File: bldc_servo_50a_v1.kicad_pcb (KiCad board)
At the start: 2 copper layers, 50 parts, among them J1 CAN_JST-1, J2 CAN_JST-2, J3 Encoder_JST_1, J4 Encoder_JST_2, J5 Fan_JST, Q1 BSC010N04LS, Q2 BSC010N04LS, Q3 BSC010N04LS, Q4 BSC010N04LS, Q5 BSC010N04LS, Q6 BSC010N04LS, U1 LM3480-3.3_Yet to decide, U2 SN65HVD230, U3 STM32G431CBT6

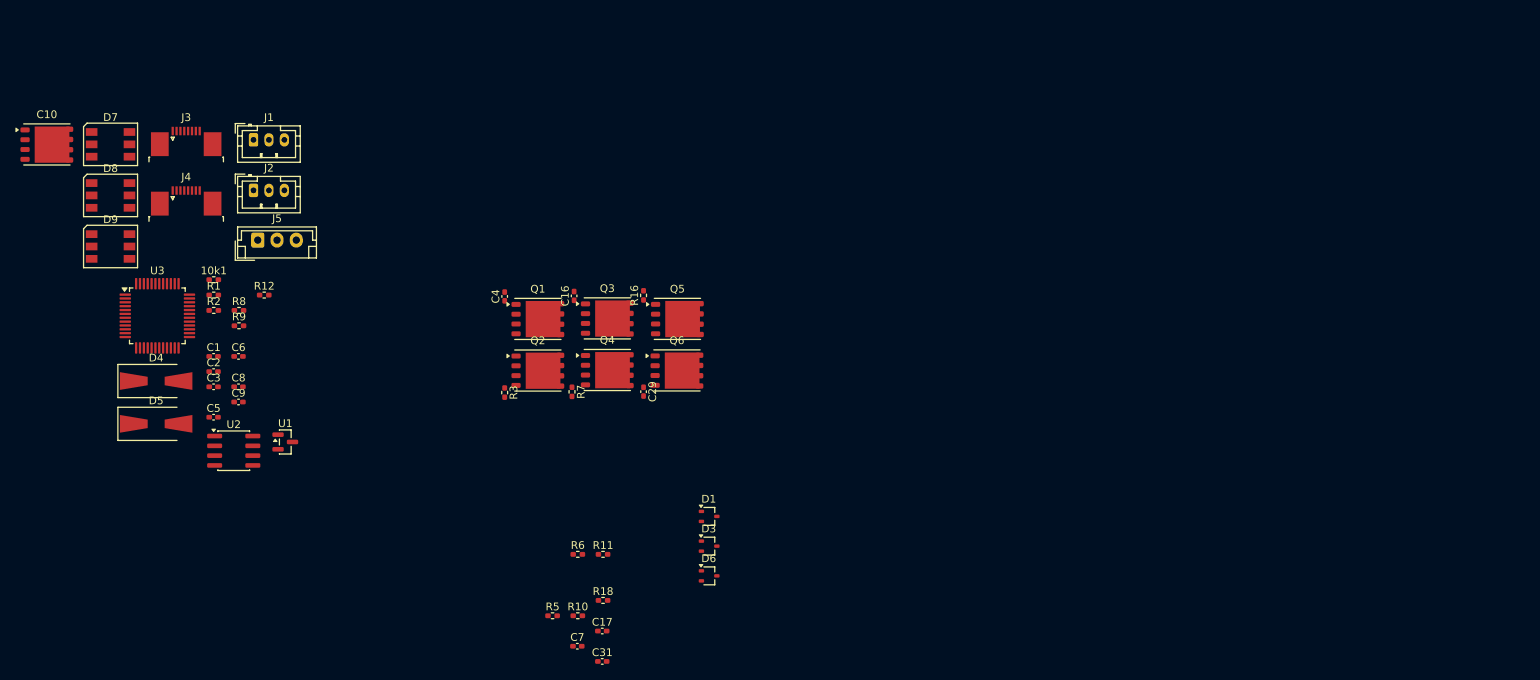
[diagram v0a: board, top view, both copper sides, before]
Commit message: FETs placed
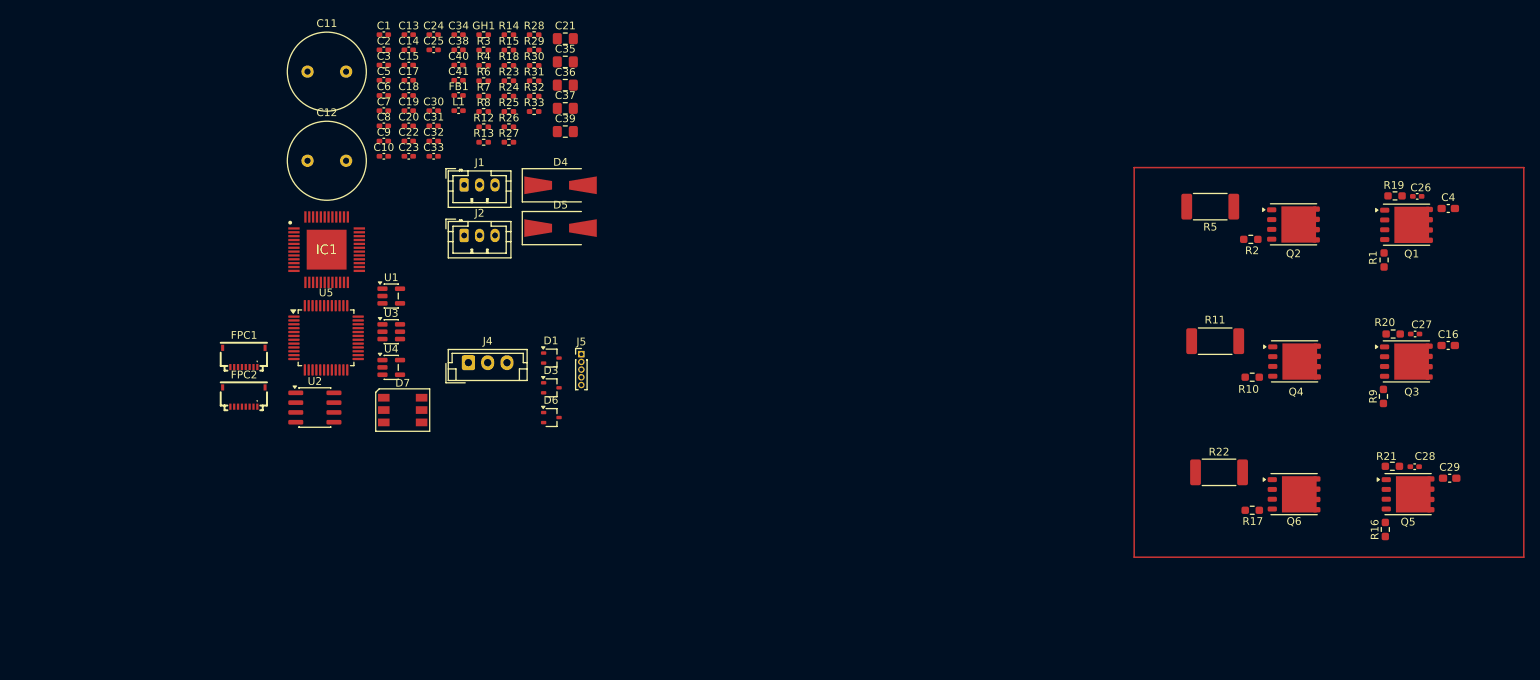
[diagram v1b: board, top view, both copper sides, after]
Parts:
- removed 10k1: R_Small, Resistor_SMD:R_0402_1005Metric_Pad0.72x0.64mm_HandSolder
- removed D8, D9: WS2812, LED_SMD:LED_WS2812_PLCC6_5.0x5.0mm_P1.6mm
- removed J3: Encoder_JST_1, Connector_FFC-FPC:TE_0-1734839-8_1x08-1MP_P0.5mm_Horizontal
- added C11: 470u, Capacitor_THT:C_Radial_D10.0mm_H16.0mm_P5.00mm, F.Cu at (74.4, 25.0)
- added C12: 470u, Capacitor_THT:C_Radial_D10.0mm_H16.0mm_P5.00mm, F.Cu at (74.4, 36.5)
- added C13: 1u, Capacitor_SMD:C_0402_1005Metric_Pad0.74x0.62mm_HandSolder, F.Cu at (87.6, 20.2)
- added C14: 0.1u, Capacitor_SMD:C_0402_1005Metric_Pad0.74x0.62mm_HandSolder, F.Cu at (87.6, 22.2)
- added C15: 0.01u, Capacitor_SMD:C_0402_1005Metric_Pad0.74x0.62mm_HandSolder, F.Cu at (87.6, 24.1)
- added C18: 1u, Capacitor_SMD:C_0402_1005Metric_Pad0.74x0.62mm_HandSolder, F.Cu at (87.6, 28.1)
- added C19: 1u, Capacitor_SMD:C_0402_1005Metric_Pad0.74x0.62mm_HandSolder, F.Cu at (87.6, 30.1)
- added C20: 100n, Capacitor_SMD:C_0402_1005Metric_Pad0.74x0.62mm_HandSolder, F.Cu at (87.6, 32.0)
- added C21: 10u, Capacitor_SMD:C_0805_2012Metric_Pad1.18x1.45mm_HandSolder, F.Cu at (107.9, 20.7)
- added C22: 100n, Capacitor_SMD:C_0402_1005Metric_Pad0.74x0.62mm_HandSolder, F.Cu at (87.6, 34.0)
- added C23: 100n, Capacitor_SMD:C_0402_1005Metric_Pad0.74x0.62mm_HandSolder, F.Cu at (87.6, 36.0)
- added C24: 100n, Capacitor_SMD:C_0402_1005Metric_Pad0.74x0.62mm_HandSolder, F.Cu at (90.8, 20.2)
- added C25: 100n, Capacitor_SMD:C_0402_1005Metric_Pad0.74x0.62mm_HandSolder, F.Cu at (90.8, 22.2)
- added C26: 22n, Capacitor_SMD:C_0402_1005Metric_Pad0.74x0.62mm_HandSolder, F.Cu at (218.3, 41.2)
- added C27: 22n, Capacitor_SMD:C_0402_1005Metric_Pad0.74x0.62mm_HandSolder, F.Cu at (218.0, 59.0)
- added C28: 22n, Capacitor_SMD:C_0402_1005Metric_Pad0.74x0.62mm_HandSolder, F.Cu at (217.9, 76.2)
- added C30: 10n, Capacitor_SMD:C_0402_1005Metric_Pad0.74x0.62mm_HandSolder, F.Cu at (90.8, 30.1)
- added C32: 1u, Capacitor_SMD:C_0402_1005Metric_Pad0.74x0.62mm_HandSolder, F.Cu at (90.8, 34.0)
- added C33: 100n, Capacitor_SMD:C_0402_1005Metric_Pad0.74x0.62mm_HandSolder, F.Cu at (90.8, 36.0)
- added C34: 100n, Capacitor_SMD:C_0402_1005Metric_Pad0.74x0.62mm_HandSolder, F.Cu at (94.0, 20.2)
- added C35: 10u, Capacitor_SMD:C_0805_2012Metric_Pad1.18x1.45mm_HandSolder, F.Cu at (107.9, 23.7)
- added C36: 10u, Capacitor_SMD:C_0805_2012Metric_Pad1.18x1.45mm_HandSolder, F.Cu at (107.9, 26.8)
- added C37: 10u, Capacitor_SMD:C_0805_2012Metric_Pad1.18x1.45mm_HandSolder, F.Cu at (107.9, 29.8)
- added C38: 100n, Capacitor_SMD:C_0402_1005Metric_Pad0.74x0.62mm_HandSolder, F.Cu at (94.0, 22.2)
- added C39: 10u, Capacitor_SMD:C_0805_2012Metric_Pad1.18x1.45mm_HandSolder, F.Cu at (107.9, 32.8)
- added C40: 100n, Capacitor_SMD:C_0402_1005Metric_Pad0.74x0.62mm_HandSolder, F.Cu at (94.0, 24.1)
- added C41: 100n, Capacitor_SMD:C_0402_1005Metric_Pad0.74x0.62mm_HandSolder, F.Cu at (94.0, 26.1)
- added FB1: FB, Capacitor_SMD:C_0402_1005Metric_Pad0.74x0.62mm_HandSolder, F.Cu at (94.0, 28.1)
- added FPC1: External sensor, HCTL HC-FPC-05-09-8RLTAG_8pin connector:FPC-SMD_8P-P0.50_HC-FPC-05-09-8RLTAG, F.Cu at (66.2, 62.0)
- added FPC2: External sensor, HCTL HC-FPC-05-09-8RLTAG_8pin connector:FPC-SMD_8P-P0.50_HC-FPC-05-09-8RLTAG, F.Cu at (66.2, 67.2)
- added GH1: 10k, Resistor_SMD:R_0402_1005Metric_Pad0.72x0.64mm_HandSolder, F.Cu at (97.3, 20.2)
- added IC1: DRV8305NQPHPRQ1, DRV8305NQPHPRQ1:QFP50P900X900X120-49N, F.Cu at (76.9, 48.1)
- added L1: 3.3uH, Capacitor_SMD:C_0402_1005Metric_Pad0.74x0.62mm_HandSolder, F.Cu at (94.0, 30.1)
- added R13: 5k, Resistor_SMD:R_0402_1005Metric_Pad0.72x0.64mm_HandSolder, F.Cu at (97.3, 34.1)
- added R14: 34.8k, Resistor_SMD:R_0402_1005Metric_Pad0.72x0.64mm_HandSolder, F.Cu at (100.5, 20.2)
- added R15: 5k, Resistor_SMD:R_0402_1005Metric_Pad0.72x0.64mm_HandSolder, F.Cu at (100.5, 22.2)
- added R17: 10, Resistor_SMD:R_0603_1608Metric_Pad0.98x0.95mm_HandSolder, F.Cu at (196.9, 81.9)
- added R19: 10, Resistor_SMD:R_0603_1608Metric_Pad0.98x0.95mm_HandSolder, F.Cu at (215.4, 41.1)
- added R20: 10, Resistor_SMD:R_0603_1608Metric_Pad0.98x0.95mm_HandSolder, F.Cu at (215.2, 59.0)
- added R21: 10, Resistor_SMD:R_0603_1608Metric_Pad0.98x0.95mm_HandSolder, F.Cu at (215.1, 76.2)
- added R22: 1m, Resistor_SMD:R_2512_6332Metric_Pad1.40x3.35mm_HandSolder, F.Cu at (192.6, 76.9)
- added R23: 100k, Resistor_SMD:R_0402_1005Metric_Pad0.72x0.64mm_HandSolder, F.Cu at (100.5, 26.2)
- added R24: 13.7k, Resistor_SMD:R_0402_1005Metric_Pad0.72x0.64mm_HandSolder, F.Cu at (100.5, 28.2)
- added R25: 34.8k, Resistor_SMD:R_0402_1005Metric_Pad0.72x0.64mm_HandSolder, F.Cu at (100.5, 30.2)
- added R26: 5k, Resistor_SMD:R_0402_1005Metric_Pad0.72x0.64mm_HandSolder, F.Cu at (100.5, 32.2)
- added R27: 34.8k, Resistor_SMD:R_0402_1005Metric_Pad0.72x0.64mm_HandSolder, F.Cu at (100.5, 34.1)
- added R28: 5k, Resistor_SMD:R_0402_1005Metric_Pad0.72x0.64mm_HandSolder, F.Cu at (103.8, 20.2)
- added R29: 10k1, Resistor_SMD:R_0402_1005Metric_Pad0.72x0.64mm_HandSolder, F.Cu at (103.8, 22.2)
- added R30: 34.8k, Resistor_SMD:R_0402_1005Metric_Pad0.72x0.64mm_HandSolder, F.Cu at (103.8, 24.2)
- added R31: 5k, Resistor_SMD:R_0402_1005Metric_Pad0.72x0.64mm_HandSolder, F.Cu at (103.8, 26.2)
- added R32: 34.8k, Resistor_SMD:R_0402_1005Metric_Pad0.72x0.64mm_HandSolder, F.Cu at (103.8, 28.2)
- added R33: 5k, Resistor_SMD:R_0402_1005Metric_Pad0.72x0.64mm_HandSolder, F.Cu at (103.8, 30.2)
- added R4: 10k, Resistor_SMD:R_0402_1005Metric_Pad0.72x0.64mm_HandSolder, F.Cu at (97.3, 24.2)
- added U4: TPS2051BDBV, Package_TO_SOT_SMD:SOT-23-5, F.Cu at (85.3, 63.3)
- added U5: STM32G431CBT6, Package_QFP:LQFP-48_7x7mm_P0.5mm, F.Cu at (76.8, 59.5)
- C10: footprint Package_SON:Infineon_PG-TDSON-8_6.15x5.15mm -> Capacitor_SMD:C_0402_1005Metric_Pad0.74x0.62mm_HandSolder
- C16, C29, C4: footprint Capacitor_SMD:C_0402_1005Metric_Pad0.74x0.62mm_HandSolder -> Capacitor_SMD:C_0603_1608Metric_Pad1.08x0.95mm_HandSolder
- J4: value Encoder_JST_2 -> Fan_JST; footprint Connector_FFC-FPC:TE_0-1734839-8_1x08-1MP_P0.5mm_Horizontal -> Connector_JST:JST_EH_B3B-EH-A_1x03_P2.50mm_Vertical
- J5: value Fan_JST -> SWD; footprint Connector_JST:JST_EH_B3B-EH-A_1x03_P2.50mm_Vertical -> Connector_PinHeader_1.00mm:PinHeader_1x05_P1.00mm_Vertical
- R1, R2: value 10k -> 10; footprint Resistor_SMD:R_0402_1005Metric_Pad0.72x0.64mm_HandSolder -> Resistor_SMD:R_0603_1608Metric_Pad0.98x0.95mm_HandSolder
- R10: value 34.8k -> 10; footprint Resistor_SMD:R_0402_1005Metric_Pad0.72x0.64mm_HandSolder -> Resistor_SMD:R_0603_1608Metric_Pad0.98x0.95mm_HandSolder
- R11: value 5k -> 1m; footprint Resistor_SMD:R_0402_1005Metric_Pad0.72x0.64mm_HandSolder -> Resistor_SMD:R_2512_6332Metric_Pad1.40x3.35mm_HandSolder
- R12: value 120 -> 34.8k
- R16: value 1m -> 10; footprint Resistor_SMD:R_0402_1005Metric_Pad0.72x0.64mm_HandSolder -> Resistor_SMD:R_0603_1608Metric_Pad0.98x0.95mm_HandSolder
- R18: value 5k -> 120
- R3: value 1m -> 10k
- R5: value 34.8k -> 1m; footprint Resistor_SMD:R_0402_1005Metric_Pad0.72x0.64mm_HandSolder -> Resistor_SMD:R_2512_6332Metric_Pad1.40x3.35mm_HandSolder
- R6: value 5k -> 100
- R7: value 1m -> 34.8k
- R8: value 34.8k -> 5k
- R9: value 5k -> 10; footprint Resistor_SMD:R_0402_1005Metric_Pad0.72x0.64mm_HandSolder -> Resistor_SMD:R_0603_1608Metric_Pad0.98x0.95mm_HandSolder
- U1: value LM3480-3.3_Yet to decide -> TLV75533PDBV; footprint Package_TO_SOT_SMD:SOT-23 -> Package_TO_SOT_SMD:SOT-23-5
- U3: value STM32G431CBT6 -> LMR51430; footprint Package_QFP:LQFP-48_7x7mm_P0.5mm -> Package_TO_SOT_SMD:SOT-23-6
- moved R1 151.8 mm to (214.0, 49.4), turned to 90 degrees
- moved R9 148.6 mm to (213.9, 67.1), turned to 90 degrees
- moved R2 134.7 mm to (196.7, 46.7)
- moved C4 122.8 mm to (222.3, 42.7), turned to 0 degrees
- moved C16 113.5 mm to (222.3, 60.5), turned to 0 degrees
- moved Q1 113.2 mm to (216.9, 44.9)
- moved C29 105.1 mm to (222.5, 77.7), turned to 0 degrees
- moved Q3 103.7 mm to (216.9, 62.6)
- moved R16 100.8 mm to (214.1, 84.3)
- moved R5 100.4 mm to (191.4, 42.5), turned to 180 degrees
- moved Q2 99.8 mm to (202.2, 44.8)
- moved Q5 97.4 mm to (217.1, 79.8)
- moved R10 92.7 mm to (196.9, 64.6)
- moved Q4 89.1 mm to (202.4, 62.6)
- moved R11 84.0 mm to (192.1, 59.9), turned to 180 degrees
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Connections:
- C17 pad 1: /BSENSE -> +3.3V
- C17 pad 2: GND -> Net-(U1-GND)
- D7 pad 1: Net-(D7-DOUT) -> unconnected-(D7-DOUT-Pad1)
- J4 pad 1: +5V -> /FAN
- J4 pad 2: GND -> +5V
- J4 pad 3: /MOSI -> GND
- J5 pad 1: /FAN -> +3.3V
- J5 pad 2: +5V -> /SWDIO
- J5 pad 3: GND -> /SWCLK
- Q1 pad 4: /GH_A -> Net-(Q1-G)
- Q2 pad 4: /GL_A -> Net-(Q2-G)
- Q3 pad 4: /GH_B -> Net-(Q3-G)
- Q4 pad 4: /GL_B -> Net-(Q4-G)
- Q5 pad 4: /GH_C -> Net-(Q5-G)
- Q6 pad 4: /GL_C -> Net-(Q6-G)
- R1 pad 1: +3.3V -> /GH_A
- R1 pad 2: /NFAULT -> Net-(Q1-G)
- R10 pad 1: /PHASE_B -> /GL_B
- R10 pad 2: /BSENSE -> Net-(Q4-G)
- R11 pad 1: /BSENSE -> /SL_B
- R12 pad 1: Net-(JP1-A) -> PVDD
- R12 pad 2: /CAN_L -> /PVDDSENSE
- R16 pad 1: /SL_C -> /GH_C
- R16 pad 2: GND -> Net-(Q5-G)
- R18 pad 1: /CSENSE -> Net-(JP1-A)
- R18 pad 2: GND -> /CAN_L
- R2 pad 1: +3.3V -> /GL_A
- R2 pad 2: /PWRGD -> Net-(Q2-G)
- R3 pad 1: /SL_A -> +3.3V
- R3 pad 2: GND -> /NFAULT
- R5 pad 1: /PHASE_A -> /SL_A
- R5 pad 2: /ASENSE -> GND
- R6 pad 1: /ASENSE -> PVDD
- R6 pad 2: GND -> Net-(IC1-VDRAIN)
- R7 pad 1: /SL_B -> /PHASE_A
- R7 pad 2: GND -> /ASENSE
- R8 pad 1: PVDD -> /ASENSE
- R8 pad 2: /PVDDSENSE -> GND
- R9 pad 1: /PVDDSENSE -> /GH_B
- R9 pad 2: GND -> Net-(Q3-G)
- U1 pad 1: +3.3V -> +5V
- U1 pad 2: +5V -> Net-(U1-GND)
- U1 pad 3: GND -> +5V
- U3 pad 1: +3.3V -> GND
- U3 pad 2: /EN_GATE -> /5V_SW
- U3 pad 3: /WAKE -> PVDD
- U3 pad 4: unconnected-(U3-PC15-Pad4) -> /5V_FB
- U3 pad 5: /SH_B_SENSE -> PVDD
- U3 pad 6: /PVDDSENSE -> /5V_BOOT

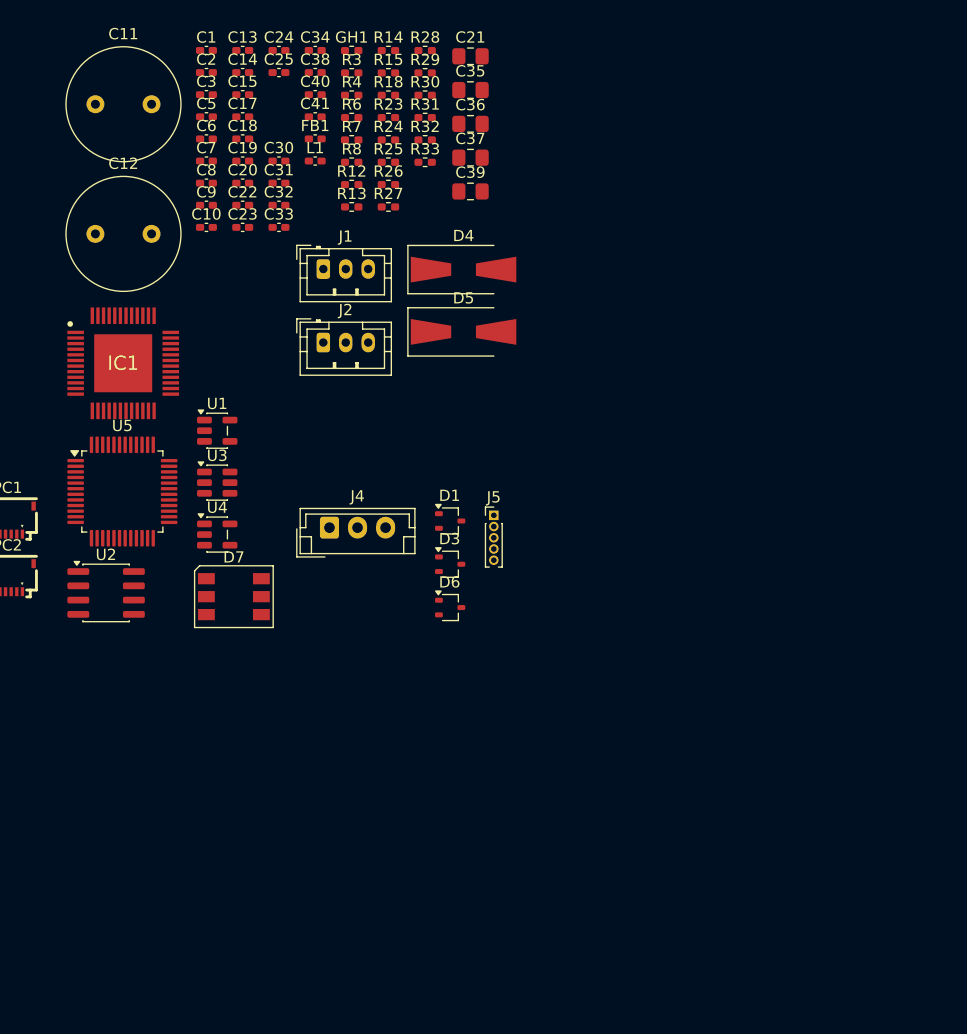
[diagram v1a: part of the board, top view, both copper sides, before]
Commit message: Basic tentative component placement for MCU and DRV
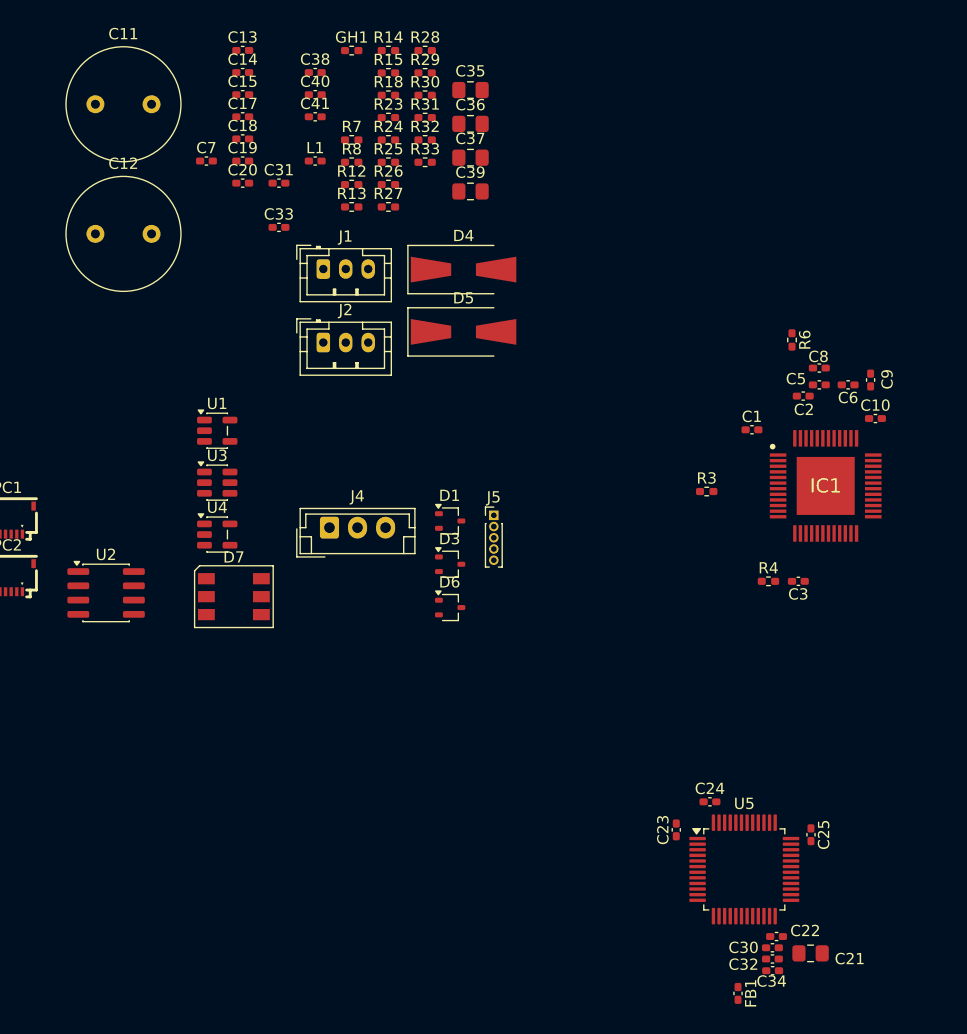
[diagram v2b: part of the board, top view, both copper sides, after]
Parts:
- moved C34 91.5 mm to (134.8, 102.2)
- moved C21 85.5 mm to (138.2, 100.6), turned to 180 degrees
- moved FB1 84.9 mm to (131.7, 104.2), turned to -90 degrees
- moved C25 82.8 mm to (138.2, 90.1), turned to -90 degrees
- moved C30 82.7 mm to (134.8, 100.1)
- moved C22 80.7 mm to (135.1, 99.1), turned to 180 degrees
- moved C32 80.3 mm to (134.8, 101.1)
- moved C24 77.2 mm to (129.2, 87.1)
- moved C3 68.3 mm to (137.1, 67.5), turned to 180 degrees
- moved C23 66.1 mm to (126.2, 89.6), turned to 90 degrees
- moved U5 64.8 mm to (132.2, 93.2)
- moved IC1 63.5 mm to (139.5, 59.0)
- moved C10 62.0 mm to (143.9, 53.0)
- moved C6 61.2 mm to (141.5, 50.0), turned to 180 degrees
- moved C9 61.2 mm to (143.5, 49.6), turned to 90 degrees
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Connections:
- IC1 pad 23: /SL_A -> /SN1
